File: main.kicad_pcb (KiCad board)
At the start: 2 copper layers, 150 x 50 mm, 179 parts, among them J1 AC, J2 OUT0, J3 OUT1, J4 Screw_Terminal_01x03, J5 Expansion, P1 TC2030-CTX-Tag-Connect-ESP32, Q1 NCE01P18K, Q2 TSF7N80M, Q3 2N5551, Q4 TSF7N80M, Q5 2N5551, Q6 NCE01P18K, Q7 2N5551, U1 MAX4080S, U10 AMS1117-3.3, U11 MAX485E, U12 TJA1051T, U13 TM8211, U2 ESP32-WROOM, U3 LMV324, U4 MAX4080S, U5 STCH03TR, U6 PC817X2, U7 STCH03TR, U8 PC817X2, U9 XL7005A

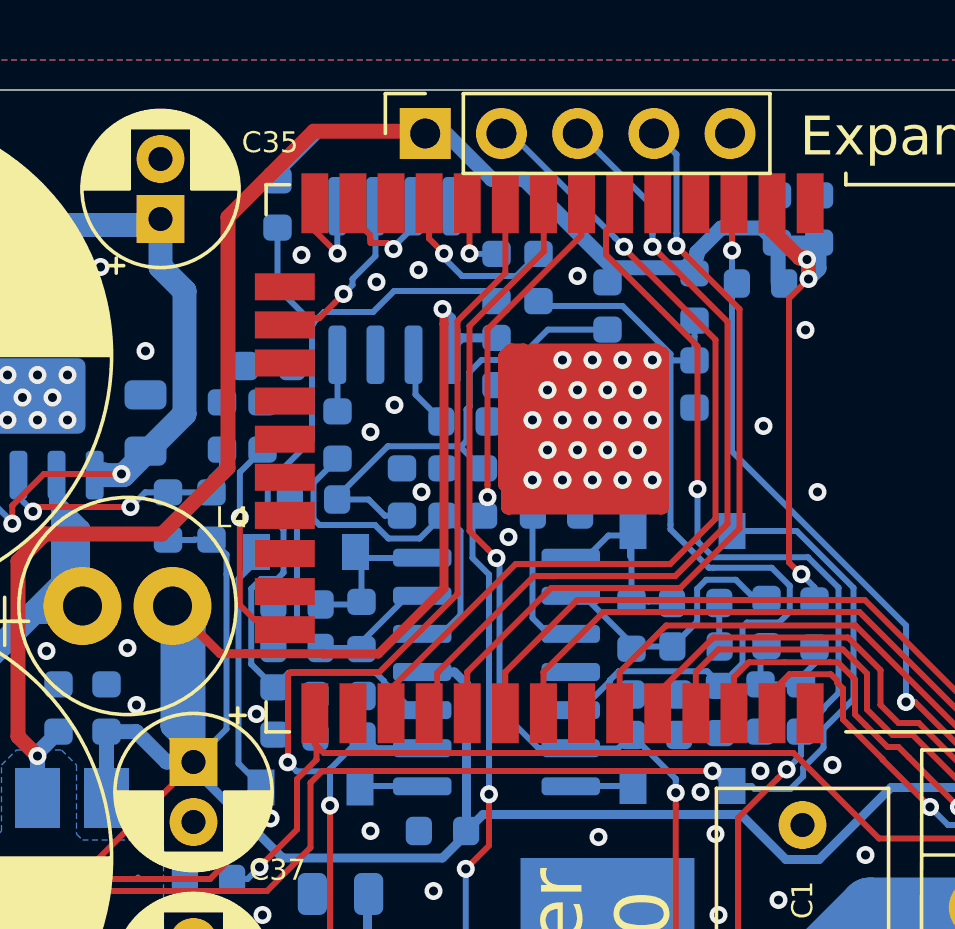
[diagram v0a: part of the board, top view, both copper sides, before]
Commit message: modified Voltage DAC bias
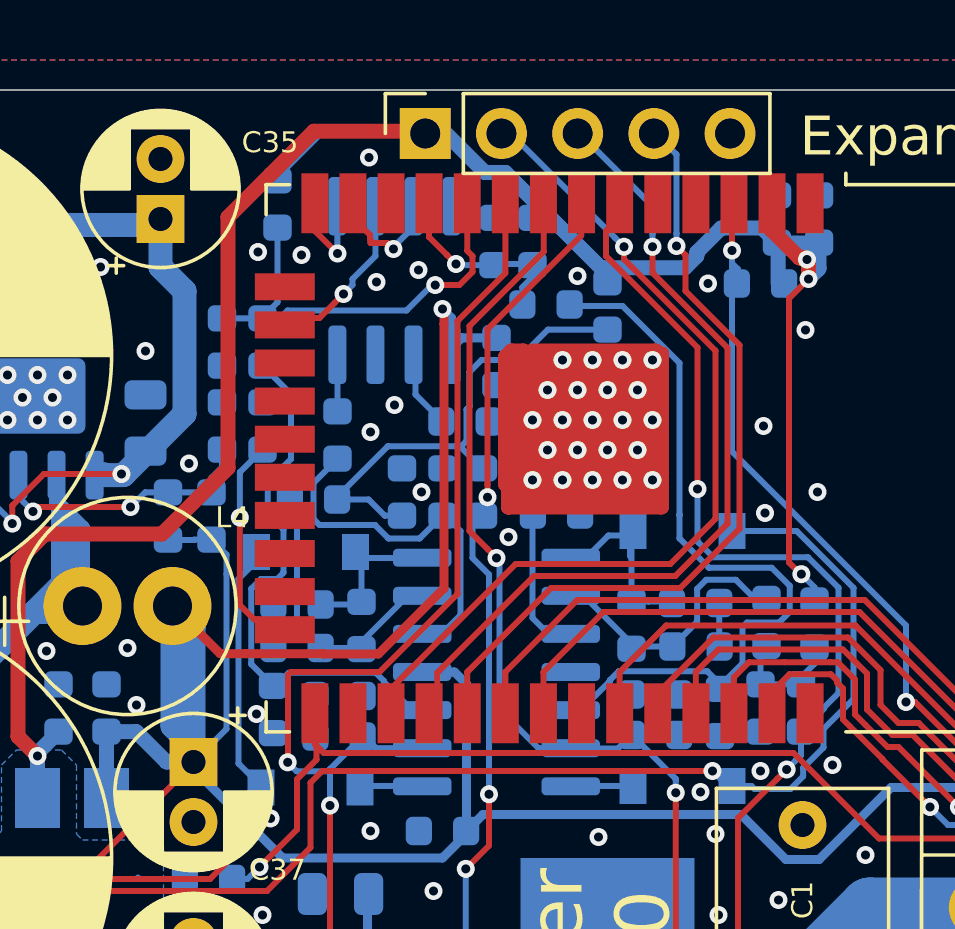
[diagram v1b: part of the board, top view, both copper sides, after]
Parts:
- moved R66 8.21 mm to (219.2, 55.0), turned to 270 degrees
- moved R55 8.09 mm to (211.5, 58.4)
- moved R65 5.71 mm to (220.5, 55.0)
- moved R64 1.74 mm to (210.2, 58.4), turned to 90 degrees
- moved R56 0.93 mm to (220.9, 57.1), turned to 180 degrees
- moved C12 0.10 mm to (226.8, 70.8)
- moved C11 0.07 mm to (211.8, 70.7), turned to 270 degrees
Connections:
- C11 pad 1: Earth -> Net-(C11-Pad1)
- C11 pad 2: USET0 -> Earth
- C12 pad 1: USET1 -> Net-(C12-Pad1)
- R55 pad 1: USET0 -> Net-(C11-Pad1)
- R55 pad 2: Net-(R55-Pad2) -> USET0
- R56 pad 1: USET1 -> Net-(C12-Pad1)
- R56 pad 2: Net-(R56-Pad2) -> USET1
- U2 pad 10: Net-(R55-Pad2) -> USET0
- U2 pad 11: Net-(R56-Pad2) -> USET1
- U3 pad 12: USET1 -> Net-(C12-Pad1)
- U3 pad 3: USET0 -> Net-(C11-Pad1)
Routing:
- net Net-(C12-Pad1): track 0.00 -> 25.0 mm
- net USET1: track 28.6 -> 6.53 mm, vias 0 -> 1
- net Net-(C11-Pad1): track 0.00 -> 18.5 mm
- net USET0: track 30.8 -> 14.6 mm, vias 0 -> 1
- net Net-(R56-Pad2): track 5.66 -> 0.00 mm, vias 1 -> 0
- net Net-(R55-Pad2): track 2.41 -> 0.00 mm, vias 1 -> 0
- net EN: track 48.5 -> 49.9 mm
- net Earth: vias 112 -> 117
